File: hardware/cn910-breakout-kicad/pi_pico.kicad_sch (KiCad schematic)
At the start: 5 parts, among them J4 RF_AGC_IN, J5 RF_AGC_OUT, J6 CAP_FG, J7 RF_SWP

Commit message: PCB work
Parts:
- J4, J5, J6, J7: footprint CN910 Breakout Footprints:Molex_0731000154_BNC_RA_THT -> CN910 Breakout Footprints:GRADCONN_RFPC-SMA28-F
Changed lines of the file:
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@@
 			)
 		)
-		(property "Footprint" "CN910 Breakout Footprints:Molex_0731000154_BNC_RA_THT"
+		(property "Footprint" "CN910 Breakout Footprints:GRADCONN_RFPC-SMA28-F"
 			(at 80.01 156.21 0)
 			(effects
@@
 			)
 		)
-		(property "Footprint" "CN910 Breakout Footprints:Molex_0731000154_BNC_RA_THT"
+		(property "Footprint" "CN910 Breakout Footprints:GRADCONN_RFPC-SMA28-F"
 			(at 48.26 181.61 0)
 			(effects
@@
 			)
 		)
-		(property "Footprint" "CN910 Breakout Footprints:Molex_0731000154_BNC_RA_THT"
+		(property "Footprint" "CN910 Breakout Footprints:GRADCONN_RFPC-SMA28-F"
 			(at 48.26 148.59 0)
 			(effects
@@
 			)
 		)
-		(property "Footprint" "CN910 Breakout Footprints:Molex_0731000154_BNC_RA_THT"
+		(property "Footprint" "CN910 Breakout Footprints:GRADCONN_RFPC-SMA28-F"
 			(at 48.26 165.1 0)
 			(effects

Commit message: Wired up scope checking SMA connectors
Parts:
- J4, J5, J6, J7: symbol Connector:Conn_Coaxial -> CN910 Breakout Symbols:RFPC-SMA28-F; MANUFACTURER (none) -> GradConn; MAXIMUM_PACKAGE_HEIGHT (none) -> 9.8mm; PARTREV (none) -> 1.0; STANDARD (none) -> Manufacturer Recommendations
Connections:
- net GND: now also J4.G1, J4.G2, J4.G3, J4.G4, J5.G1, J5.G2, J5.G3, J5.G4, J6.G1, J6.G2, J6.G3, J6.G4, J7.G1, J7.G2, J7.G3, J7.G4; no longer J4.2 (Ext), J5.2 (Ext), J6.2 (Ext), J7.2 (Ext)
- net PICO_LANC1_RX_N: now also A1.21 (GPIO16); no longer A1.2 (GPIO1)
- net PICO_LANC2_RX_N: now also A1.22 (GPIO17); no longer A1.4 (GPIO2)
- net PICO_LANC_TX: now also A1.24 (GPIO18); no longer A1.1 (GPIO0)
- net +3V3: now reaches A1.36 (3V3)
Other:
- sheet LANC Interface ports: added LANC_SIG_GPIO, XCPC_IN_GPIO; removed GPIO1, GPIO2

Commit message: Nearly finalized Sony CN910 PCB and added archives of the modified clockgen main board and CX card jig
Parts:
- A1: footprint Module:RaspberryPi_Pico_Common_Unspecified -> Module:RaspberryPi_Pico_SMD_HandSolder
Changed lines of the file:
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@@
 			)
 		)
-		(property "Footprint" "Module:RaspberryPi_Pico_Common_Unspecified"
+		(property "Footprint" "Module:RaspberryPi_Pico_SMD_HandSolder"
 			(at 118.11 152.4 0)
 			(effects

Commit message: Refined routing
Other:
- title: (none) -> Pi Pico
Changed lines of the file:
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@@
 	(paper "A4")
 	(title_block
+		(title "Pi Pico")
+		(date "2026-04-28")
 		(company "GDH Technologies LLC")
 	)

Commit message: Refactored CN910 breakout KiCad project files, updating footprint and symbol references to "GDH" naming convention. Adjusted PCB thickness and dielectric properties for improved design accuracy. Added new adhesive layers and updated project metadata with a new variant description. Removed obsolete libraries and 3D models to streamline the project.
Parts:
- J4, J5, J6, J7: footprint CN910 Breakout Footprints:GRADCONN_RFPC-SMA28-F -> GDH Connectors:GRADCONN_RFPC-SMA28-F; symbol CN910 Breakout Symbols:RFPC-SMA28-F -> GDH Connectors:RFPC-SMA28-F
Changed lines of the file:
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@@
 	)
 	(symbol
-		(lib_id "CN910 Breakout Symbols:RFPC-SMA28-F")
+		(lib_id "GDH Connectors:RFPC-SMA28-F")
 		(at 85.09 147.32 0)
 		(mirror y)
@@
 			)
 		)
-		(property "Footprint" "CN910 Breakout Footprints:GRADCONN_RFPC-SMA28-F"
+		(property "Footprint" "GDH Connectors:GRADCONN_RFPC-SMA28-F"
 			(at 85.09 147.32 0)
 			(hide yes)
@@
 	)
 	(symbol
-		(lib_id "CN910 Breakout Symbols:RFPC-SMA28-F")
+		(lib_id "GDH Connectors:RFPC-SMA28-F")
 		(at 73.66 171.45 0)
 		(mirror y)
@@
 			)
 		)
-		(property "Footprint" "CN910 Breakout Footprints:GRADCONN_RFPC-SMA28-F"
+		(property "Footprint" "GDH Connectors:GRADCONN_RFPC-SMA28-F"
 			(at 73.66 171.45 0)
 			(hide yes)
@@
 	)
 	(symbol
-		(lib_id "CN910 Breakout Symbols:RFPC-SMA28-F")
+		(lib_id "GDH Connectors:RFPC-SMA28-F")
 		(at 45.72 148.59 0)
 		(mirror y)
@@
 			)
 		)
-		(property "Footprint" "CN910 Breakout Footprints:GRADCONN_RFPC-SMA28-F"
+		(property "Footprint" "GDH Connectors:GRADCONN_RFPC-SMA28-F"
 			(at 45.72 148.59 0)
 			(hide yes)
@@
 	)
 	(symbol
-		(lib_id "CN910 Breakout Symbols:RFPC-SMA28-F")
+		(lib_id "GDH Connectors:RFPC-SMA28-F")
 		(at 45.72 168.91 0)
 		(mirror y)
@@
 			)
 		)
-		(property "Footprint" "CN910 Breakout Footprints:GRADCONN_RFPC-SMA28-F"
+		(property "Footprint" "GDH Connectors:GRADCONN_RFPC-SMA28-F"
 			(at 45.72 168.91 0)
 			(hide yes)

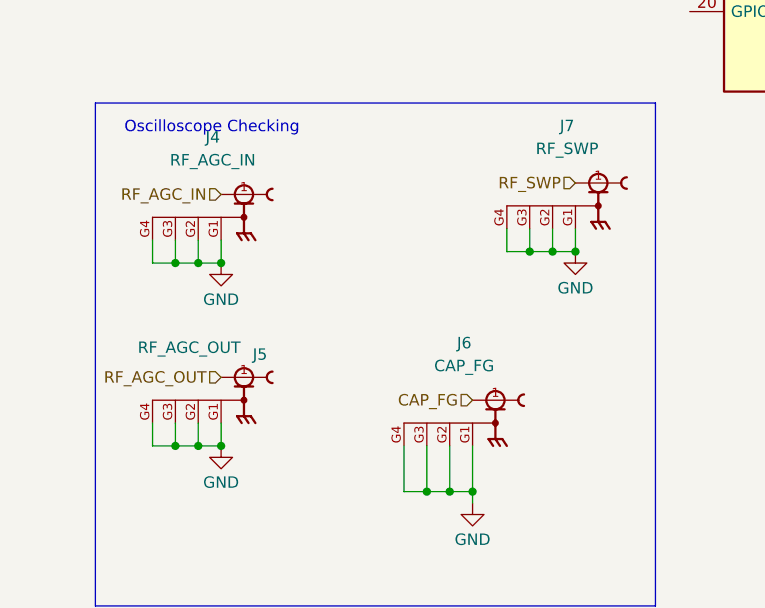
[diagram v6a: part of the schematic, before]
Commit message: Updated CN910 breakout KiCad project files with dynamic project metadata, including title, company, version, and license. Refined design rules and component properties for improved clarity and organization. Adjusted pin functions and descriptions for connectors, and removed obsolete library references. Enhanced layout with new wire connections and updated schematic components.
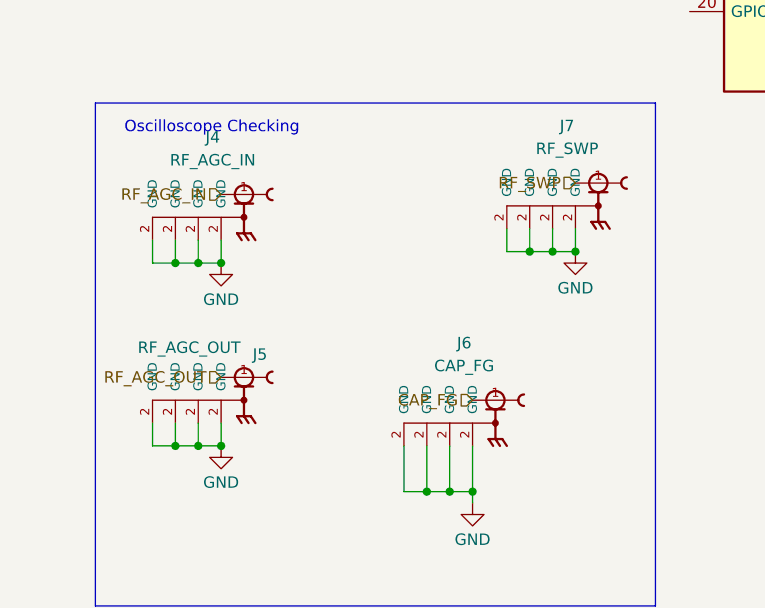
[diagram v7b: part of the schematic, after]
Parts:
- J4, J5, J6, J7: MPN (none) -> RFPC-SMA28-F; Manufacturer (none) -> GCT
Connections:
- net GND: now also J4.2 (GND), J5.2 (GND), J6.2 (GND), J7.2 (GND); no longer J4.G1, J4.G2, J4.G3, J4.G4, J5.G1, J5.G2, J5.G3, J5.G4, J6.G1, J6.G2, J6.G3, J6.G4, J7.G1, J7.G2, J7.G3, J7.G4
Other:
- company: GDH Technologies LLC -> ${proj-company}
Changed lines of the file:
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@@
 		(title "Pi Pico")
 		(date "2026-04-28")
-		(company "GDH Technologies LLC")
+		(company "${proj-company}")
 	)
 	(rectangle
@@
 			)
 		)
-		(property "Datasheet" ""
+		(property "Datasheet" "https://mm.digikey.com/Volume0/opasdata/d220001/medias/docus/6130/RFPC-SMA28-F.pdf"
 			(at 85.09 147.32 0)
 			(hide yes)
@@
 			)
 		)
-		(property "Description" "coaxial connector (BNC, SMA, SMB, SMC, Cinch/RCA, LEMO, ...)"
+		(property "Description" "SMA vertical PCB jack"
 			(at 85.09 147.32 0)
 			(hide yes)
@@
 			)
 		)
-		(pin "G3"
+		(property "Manufacturer" "GCT"
+			(at 85.09 147.32 0)
+			(hide yes)
+			(show_name no)
+			(do_not_autoplace no)
+			(effects
+				(font
+					(size 1.27 1.27)
+				)
+			)
+		)
+		(property "MPN" "RFPC-SMA28-F"
+			(at 85.09 147.32 0)
+			(hide yes)
+			(show_name no)
+			(do_not_autoplace no)
+			(effects
+				(font
+					(size 1.27 1.27)
+				)
+			)
+		)
+		(pin "2"
 		)
 		(pin "1"
 		)
-		(pin "G1"
-		)
-		(pin "G4"
-		)
-		(pin "G2"
+		(pin "2"
+		)
+		(pin "2"
+		)
+		(pin "2"
 		)
 		(instances
@@
 	)
 	(symbol
+		(lib_name "RFPC-SMA28-F_3")
 		(lib_id "GDH Connectors:RFPC-SMA28-F")
 		(at 73.66 171.45 0)
@@
 			)
 		)
-		(property "Datasheet" ""
+		(property "Datasheet" "https://mm.digikey.com/Volume0/opasdata/d220001/medias/docus/6130/RFPC-SMA28-F.pdf"
 			(at 73.66 171.45 0)
 			(hide yes)
@@
 			)
 		)
-		(property "Description" "coaxial connector (BNC, SMA, SMB, SMC, Cinch/RCA, LEMO, ...)"
+		(property "Description" "SMA vertical PCB jack"
 			(at 73.66 171.45 0)
 			(hide yes)
@@
 			)
 		)
+		(property "Manufacturer" "GCT"
+			(at 73.66 171.45 0)
+			(hide yes)
+			(show_name no)
+			(do_not_autoplace no)
+			(effects
+				(font
+					(size 1.27 1.27)
+				)
+			)
+		)
+		(property "MPN" "RFPC-SMA28-F"
+			(at 73.66 171.45 0)
+			(hide yes)
+			(show_name no)
+			(do_not_autoplace no)
+			(effects
+				(font
+					(size 1.27 1.27)
+				)
+			)
+		)
 		(pin "1"
 		)
-		(pin "G3"
-		)
-		(pin "G1"
-		)
-		(pin "G2"
-		)
-		(pin "G4"
+		(pin "2"
+		)
+		(pin "2"
+		)
+		(pin "2"
+		)
+		(pin "2"
 		)
 		(instances
@@
 	)
 	(symbol
+		(lib_name "RFPC-SMA28-F_1")
 		(lib_id "GDH Connectors:RFPC-SMA28-F")
 		(at 45.72 148.59 0)
@@
 			)
 		)
-		(property "Datasheet" ""
+		(property "Datasheet" "https://mm.digikey.com/Volume0/opasdata/d220001/medias/docus/6130/RFPC-SMA28-F.pdf"
 			(at 45.72 148.59 0)
 			(hide yes)
@@
 			)
 		)
-		(property "Description" "coaxial connector (BNC, SMA, SMB, SMC, Cinch/RCA, LEMO, ...)"
+		(property "Description" "SMA vertical PCB jack"
 			(at 45.72 148.59 0)
 			(hide yes)
@@
 			)
 		)
-		(pin "G1"
+		(property "Manufacturer" "GCT"
+			(at 45.72 148.59 0)
+			(hide yes)
+			(show_name no)
+			(do_not_autoplace no)
+			(effects
+				(font
+					(size 1.27 1.27)
+				)
+			)
+		)
+		(property "MPN" "RFPC-SMA28-F"
+			(at 45.72 148.59 0)
+			(hide yes)
+			(show_name no)
+			(do_not_autoplace no)
+			(effects
+				(font
+					(size 1.27 1.27)
+				)
+			)
+		)
+		(pin "2"
 		)
 		(pin "1"
 		)
-		(pin "G4"
-		)
-		(pin "G3"
-		)
-		(pin "G2"
+		(pin "2"
+		)
+		(pin "2"
+		)
+		(pin "2"
 		)
 		(instances
@@
 	)
 	(symbol
+		(lib_name "RFPC-SMA28-F_2")
 		(lib_id "GDH Connectors:RFPC-SMA28-F")
 		(at 45.72 168.91 0)
@@
 			)
 		)
-		(property "Datasheet" ""
+		(property "Datasheet" "https://mm.digikey.com/Volume0/opasdata/d220001/medias/docus/6130/RFPC-SMA28-F.pdf"
 			(at 45.72 168.91 0)
 			(hide yes)
@@
 			)
 		)
-		(property "Description" "coaxial connector (BNC, SMA, SMB, SMC, Cinch/RCA, LEMO, ...)"
+		(property "Description" "SMA vertical PCB jack"
 			(at 45.72 168.91 0)
 			(hide yes)
@@
 			)
 		)
+		(property "Manufacturer" "GCT"
+			(at 45.72 168.91 0)
+			(hide yes)
+			(show_name no)
+			(do_not_autoplace no)
+			(effects
+				(font
+					(size 1.27 1.27)
+				)
+			)
+		)
+		(property "MPN" "RFPC-SMA28-F"
+			(at 45.72 168.91 0)
+			(hide yes)
+			(show_name no)
+			(do_not_autoplace no)
+			(effects
+				(font
+					(size 1.27 1.27)
+				)
+			)
+		)
 		(pin "1"
 		)
-		(pin "G4"
-		)
-		(pin "G2"
-		)
-		(pin "G1"
-		)
-		(pin "G3"
+		(pin "2"
+		)
+		(pin "2"
+		)
+		(pin "2"
+		)
+		(pin "2"
 		)
 		(instances
